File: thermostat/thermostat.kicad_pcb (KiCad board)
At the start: 2 copper layers, 67.5 x 95 mm, 35 parts, among them J1 24VAC, J2 UART, J3 BOOT, J4 12VDC, J5 CTRL, U1 ESP32-WROVER-E, U2 TPS5430DDA, U3 TPS62203DBV, U4 LM324DT

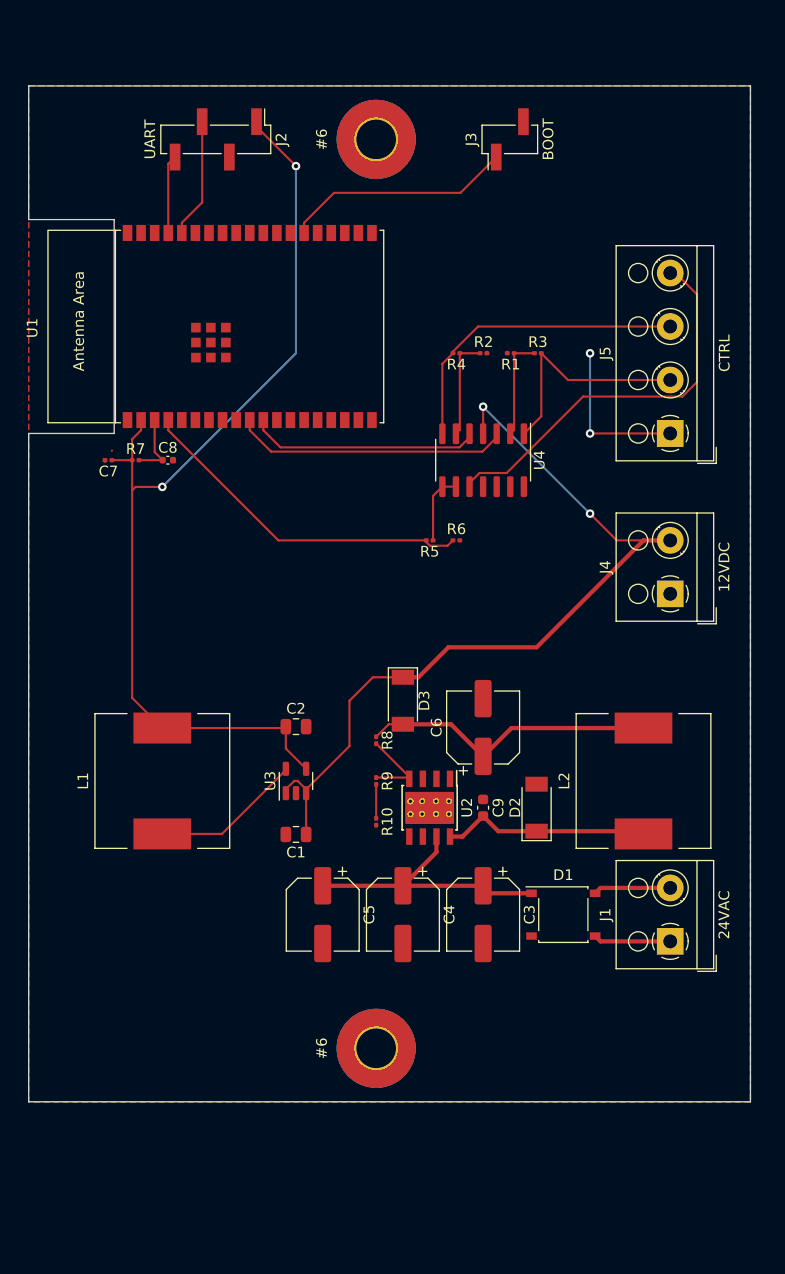
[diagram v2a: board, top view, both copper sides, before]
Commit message: Better layout with shorter debug pins
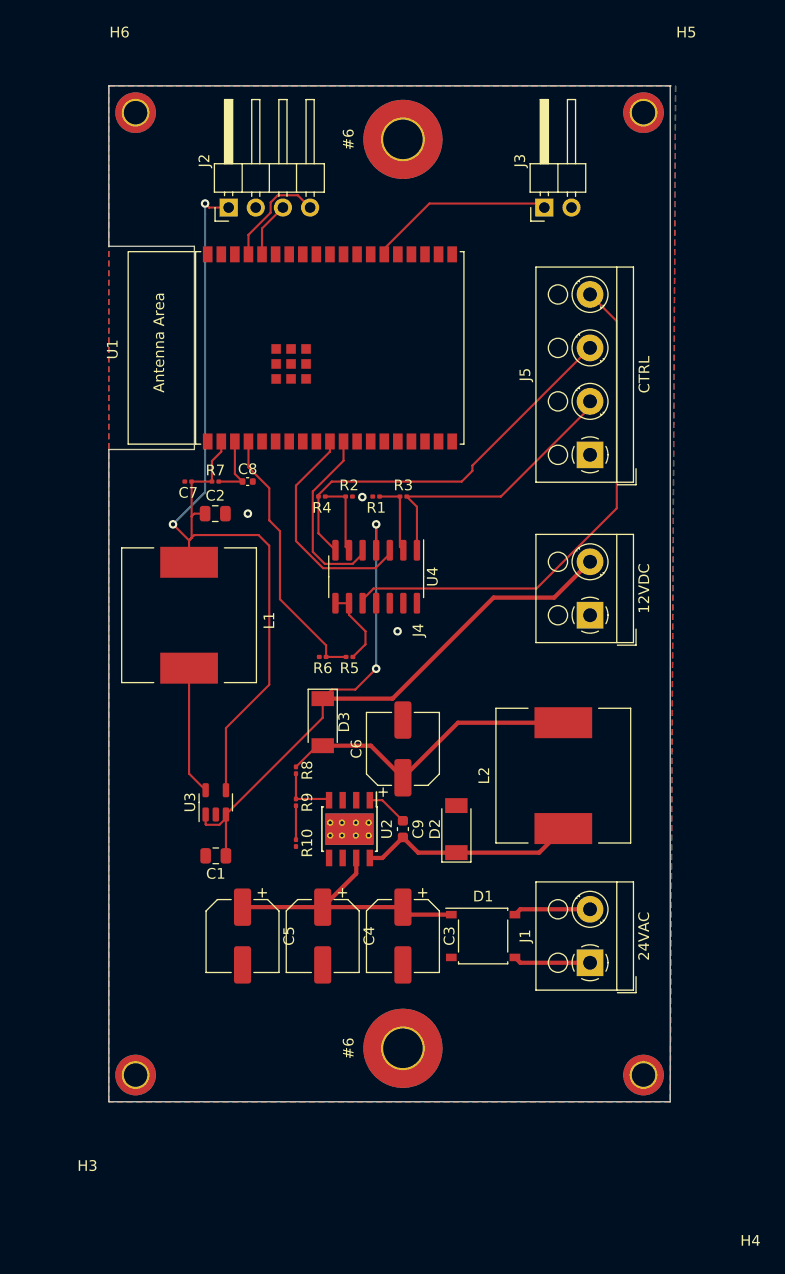
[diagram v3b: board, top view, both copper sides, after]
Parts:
- added H3: MountingHole_Pad, MountingHole:MountingHole_2.2mm_M2_DIN965_Pad_TopBottom, F.Cu at (172.5, 137.5)
- added H4: MountingHole_Pad, MountingHole:MountingHole_2.2mm_M2_DIN965_Pad_TopBottom, F.Cu at (220.0, 137.5)
- added H5: MountingHole_Pad, MountingHole:MountingHole_2.2mm_M2_DIN965_Pad_TopBottom, F.Cu at (220.0, 47.5)
- added H6: MountingHole_Pad, MountingHole:MountingHole_2.2mm_M2_DIN965_Pad_TopBottom, F.Cu at (172.5, 47.5)
- J2: footprint Connector_PinHeader_2.54mm:PinHeader_1x04_P2.54mm_Vertical_SMD_Pin1Left -> Connector_PinHeader_2.54mm:PinHeader_1x04_P2.54mm_Horizontal
- J3: footprint Connector_PinHeader_2.54mm:PinHeader_1x02_P2.54mm_Vertical_SMD_Pin1Left -> Connector_PinHeader_2.54mm:PinHeader_1x02_P2.54mm_Horizontal
- moved C2 21.3 mm to (179.9, 85.0)
- moved R1 18.4 mm to (195.0, 83.4)
- moved R3 18.4 mm to (197.5, 83.4)
- moved R4 18.4 mm to (189.9, 83.4)
- moved R2 18.4 mm to (192.5, 83.4)
- moved R6 16.6 mm to (190.0, 98.4), turned to 180 degrees
- moved L1 15.7 mm to (177.5, 94.5)
- moved U4 14.8 mm to (195.0, 90.9)
- moved R5 13.2 mm to (192.5, 98.4)
- moved R8 8.01 mm to (187.5, 109.0)
- moved C1 7.76 mm to (180.0, 117.0)
- moved C3 7.76 mm to (197.5, 124.5)
- moved C4 7.76 mm to (190.0, 124.5)
- moved C5 7.76 mm to (182.5, 124.5)
- moved C6 7.76 mm to (197.5, 107.0)
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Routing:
- net GND: track 16.0 -> 0.00 mm, vias 2 -> 3
- net /PUMP_TEMP: track 36.9 -> 48.7 mm
- net /VCC33: track 92.4 -> 83.4 mm
- net /PUMP_CTRL: track 29.9 -> 37.2 mm
- net /ADC1_CH0: track 32.3 -> 25.0 mm
- net /UART_RX: track 11.2 -> 5.18 mm
- net /FAN_CTRL: track 21.8 -> 26.6 mm
- net /DAC_1: track 25.8 -> 21.3 mm
- net /DAC_2: track 21.6 -> 17.4 mm
- net /GPIO0: track 21.5 -> 17.4 mm
- net Net-(C9-Pad1): track 0.00 -> 3.89 mm
- net /UART_TX: track 7.36 -> 10.2 mm
- net Net-(R1-Pad1): track 9.57 -> 7.06 mm
- net Net-(R2-Pad1): track 9.57 -> 7.06 mm
- net Net-(R8-Pad2): track 7.72 -> 5.50 mm
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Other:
- board size 67.5 x 95 mm -> 52.5 x 95 mm
